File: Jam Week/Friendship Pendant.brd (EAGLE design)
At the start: 66 x 66 mm, 40 parts, among them IC1 LM556D, IC2 LM556D, IC3 74AHC1G32DCK

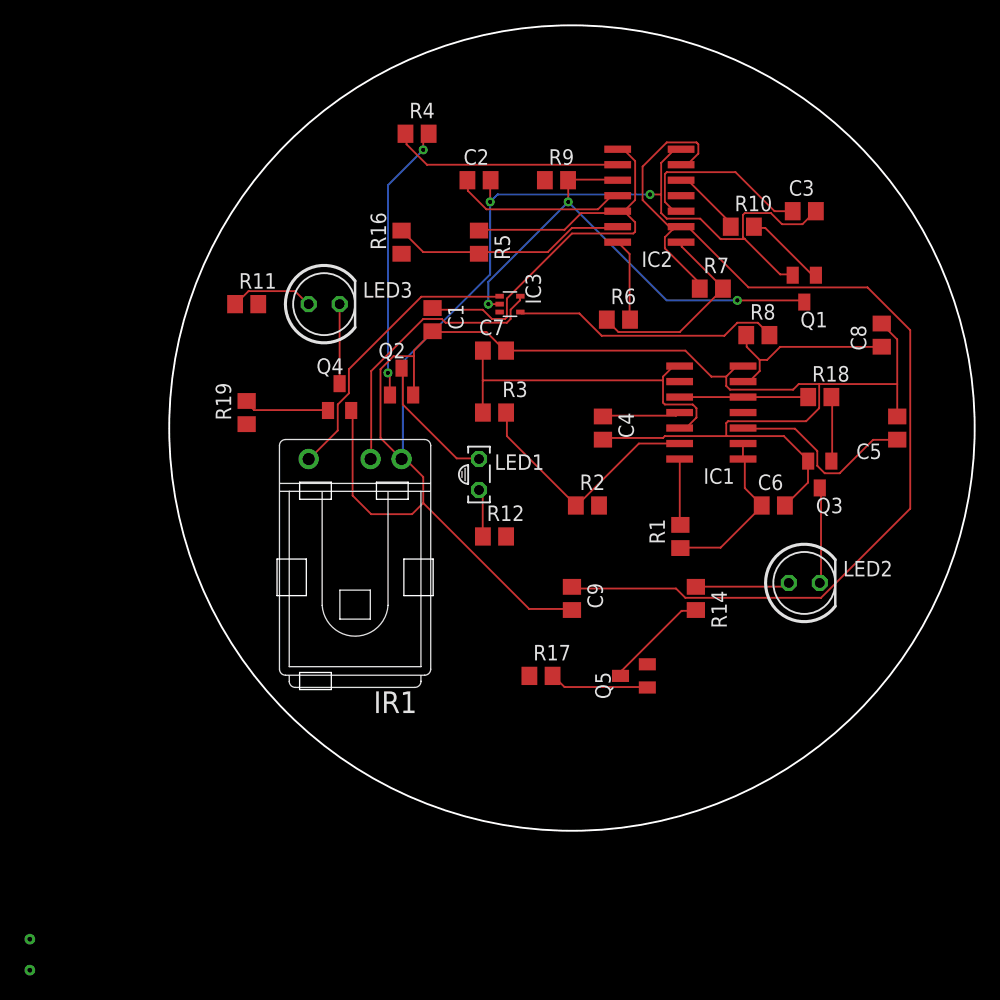
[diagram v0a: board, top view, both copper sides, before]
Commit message: Next class resolve air wire
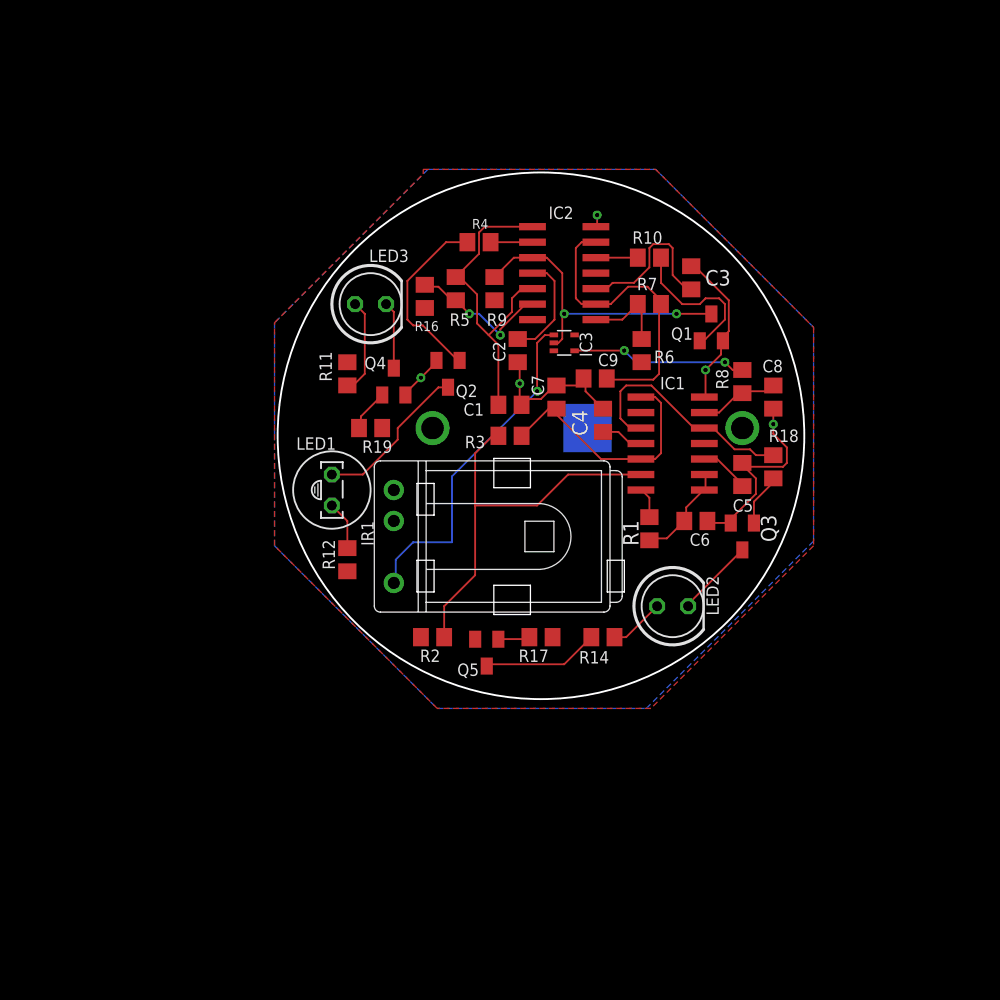
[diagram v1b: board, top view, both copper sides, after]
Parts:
- removed TP1, TP2: TEST-POINTTP_15TH_THRU, SparkFun-Connectors:TP_15TH
- added U1: 3039, 3039:3039
- moved C9 18.1 mm to (51.4, 51.1), turned to 180 degrees
- moved R2 16.7 mm to (38.1, 29.8), turned to 180 degrees
- moved C2 14.3 mm to (45.1, 53.3), turned to 270 degrees
- moved C5 13.3 mm to (63.5, 43.2)
- moved R12 12.2 mm to (31.1, 36.2), turned to 270 degrees
- moved Q5 12.2 mm to (42.5, 28.6), turned to 180 degrees
- moved LED1 12.1 mm to (29.8, 41.9)
- moved LED2 11.0 mm to (57.8, 32.4)
- moved C3 10.8 mm to (59.3, 59.3), turned to 90 degrees
- moved R4 10.2 mm to (41.9, 62.2), turned to 180 degrees
- moved R19 10.2 mm to (33.0, 47.0), turned to 180 degrees
- moved C8 10.2 mm to (66.0, 49.5), turned to 270 degrees
- moved R9 10.2 mm to (43.2, 58.4), turned to 90 degrees
- moved R11 10.0 mm to (31.1, 51.4), turned to 90 degrees
- moved IC2 9.44 mm to (48.9, 59.7)
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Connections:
- removed net N$15: IC2.14, R6.2
- removed net N$20: R12.2
- removed net N$22: IC1.4
- removed net N$25: R2.2
- removed net N$33: Q5.2
- removed net N$37: R16.1
- removed net N$38: R11.2
- removed net N$39: TP1.P$1
- net 0: now also U1.3; no longer TP2.P$1
- net VCC: now also IC1.4, IC2.14, Q5.2, R11.2, R12.2, R16.1, R2.2, R6.2, R9.1, U1.1, U1.2
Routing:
- net 0: track 203.6 -> 49.7 mm, vias 2 -> 5
- net N$16: track 90.2 -> 24.9 mm
- net VCC: track 22.9 -> 0.00 mm
- net N$4: track 40.8 -> 25.2 mm, vias 3 -> 2
- net SIGNAL: track 18.9 -> 3.44 mm
- net N$35: track 41.9 -> 27.0 mm
- net N$1: track 20.6 -> 33.3 mm
- net N$18: track 16.0 -> 4.13 mm
- net N$2: track 16.7 -> 7.04 mm
- net ENABLE: track 10.5 -> 19.3 mm
- net N$17: track 15.6 -> 6.76 mm
- net N$24: track 29.2 -> 21.2 mm
- net N$10: track 22.9 -> 15.1 mm, vias 2 -> 0
- net N$3: track 22.1 -> 14.4 mm, vias 0 -> 2
- net N$36: track 19.4 -> 12.1 mm, vias 0 -> 2
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- added copper zone on layer 16, net 0
- added copper zone on layer 1, net VCC
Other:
- board size 66 x 66 mm -> 43.2 x 43.2 mm

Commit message: Almost done,
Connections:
- removed net N$26: R19.1
- removed net N$32: R17.1
- net BLINK: now also R17.1, R19.1
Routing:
- net BLINK: track 0.00 -> 42.8 mm, vias 0 -> 3
- net ENABLE: track 19.3 -> 15.2 mm, vias 0 -> 2
- net 0: track 49.7 -> 45.5 mm, vias 5 -> 6
- net N$16: track 24.9 -> 22.0 mm
- net N$24: track 21.2 -> 22.7 mm
- net N$11: track 28.1 -> 28.6 mm, vias 1 -> 0

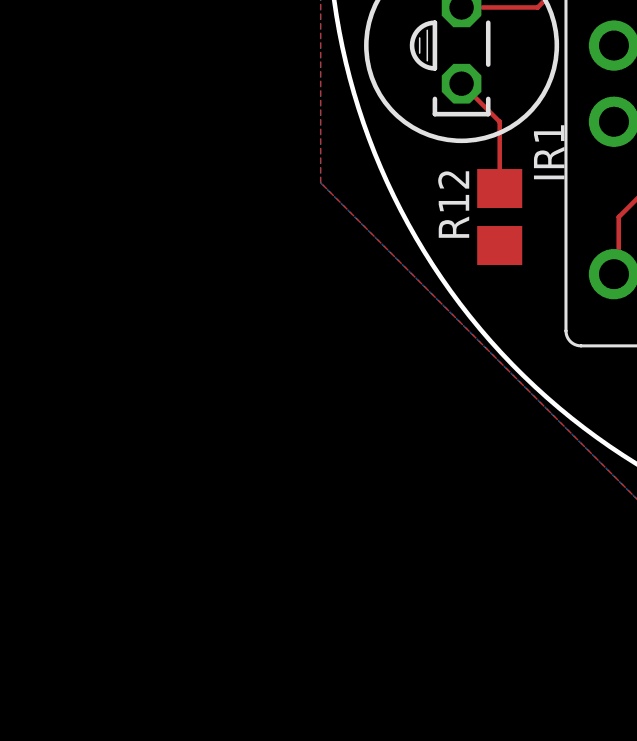
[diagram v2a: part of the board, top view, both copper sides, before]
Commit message: added switch and ordered without switch
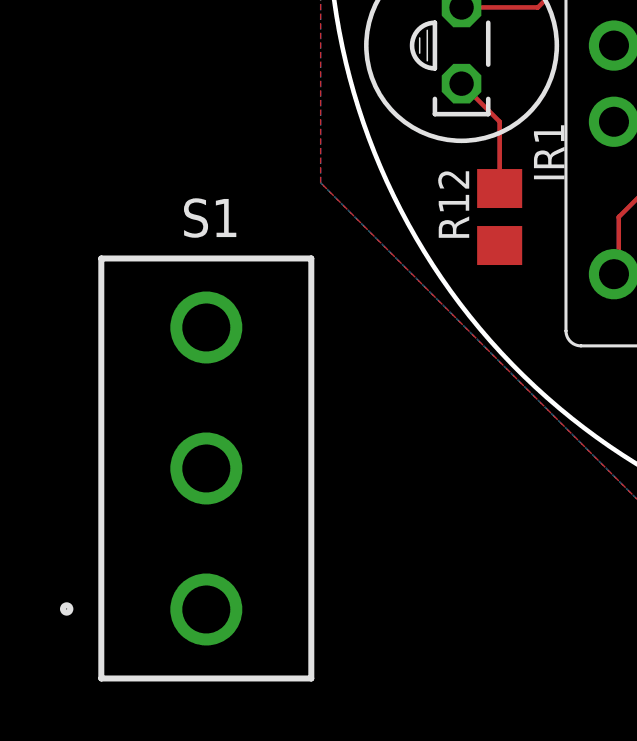
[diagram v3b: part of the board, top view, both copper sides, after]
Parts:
- added S1: CS12ANW03, CS12ANW03:CS12ANW03
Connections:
- new net N$15: S1.2, U1.1, U1.2
- net VCC: now also S1.3; no longer U1.1, U1.2
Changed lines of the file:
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@@
 <attribute name="VALUE" x="51.251" y="48.316" size="1.27" layer="28" rot="MR0" align="center"/>
+</element>
+<element name="S1" library="CS12ANW03" package="CS12ANW03" value="CS12ANW03" x="21.336" y="27.813" smashed="yes">
+<attribute name="ALLIED_NUMBER" value="70228233" x="21.336" y="27.813" size="1.778" layer="27" display="off"/>
+<attribute name="ALLIED_PRICE-STOCK" value="https://www.alliedelec.com/nkk-switches-cs12anw03/70228233/" x="21.336" y="27.813" size="1.778" layer="27" display="off"/>
+<attribute name="DESCRIPTION" value="NKK SWITCHES - CS12ANW03 - SWITCH, SLIDE, SPDT, 3A, 250V, TH" x="21.336" y="27.813" size="1.778" layer="27" display="off"/>
+<attribute name="HEIGHT" value="mm" x="21.336" y="27.813" size="1.778" layer="27" display="off"/>
+<attribute name="MANUFACTURER_NAME" value="NKK Switches" x="21.336" y="27.813" size="1.778" layer="27" display="off"/>
+<attribute name="MANUFACTURER_PART_NUMBER" value="CS12ANW03" x="21.336" y="27.813" size="1.778" layer="27" display="off"/>
+<attribute name="MOUSER_PART_NUMBER" value="633-CS12ANW03" x="21.336" y="27.813" size="1.778" layer="27" display="off"/>
+<attribute name="MOUSER_PRICE-STOCK" value="https://www.mouser.com/Search/Refine.aspx?Keyword=633-CS12ANW03" x="21.336" y="27.813" size="1.778" layer="27" display="off"/>
+<attribute name="NAME" x="21.484" y="36.162" size="1.27" layer="25" align="center"/>
+<attribute name="RS_PART_NUMBER" value="1251847" x="21.336" y="27.813" size="1.778" layer="27" display="off"/>
+<attribute name="RS_PRICE-STOCK" value="http://uk.rs-online.com/web/p/products/1251847" x="21.336" y="27.813" size="1.778" layer="27" display="off"/>
+<attribute name="VALUE" x="20.722" y="35.781" size="1.27" layer="27" align="center"/>
 </element>
 </elements>
@@
 <contactref element="IC3" pad="5"/>
 <contactref element="IR1" pad="VS"/>
-<contactref element="U1" pad="1"/>
-<contactref element="U1" pad="2"/>
 <contactref element="R9" pad="1"/>
 <contactref element="R12" pad="2"/>
@@
 <contactref element="IC2" pad="14"/>
 <contactref element="R6" pad="2"/>
+<contactref element="S1" pad="3"/>
+<wire x1="55.245" y1="52.39" x2="60.385" y2="45.72" width="0" layer="19" extent="1-1"/>
+<wire x1="49.745" y1="54.625" x2="55.245" y2="52.39" width="0" layer="19" extent="1-1"/>
+<wire x1="46.295" y1="55.88" x2="49.745" y2="54.625" width="0" layer="19" extent="1-1"/>
+<wire x1="43.18" y1="57.47" x2="46.295" y2="55.88" width="0" layer="19" extent="1-1"/>
+<wire x1="37.465" y1="56.835" x2="43.18" y2="57.47" width="0" layer="19" extent="1-1"/>
+<wire x1="31.115" y1="52.385" x2="37.465" y2="56.835" width="0" layer="19" extent="1-1"/>
+<wire x1="34.925" y1="39.37" x2="31.115" y2="52.385" width="0" layer="19" extent="1-1"/>
+<wire x1="31.115" y1="35.245" x2="34.925" y2="39.37" width="0" layer="19" extent="1-1"/>
+<wire x1="37.15" y1="29.845" x2="31.115" y2="35.245" width="0" layer="19" extent="1-1"/>
+<wire x1="41.595" y1="29.675" x2="37.15" y2="29.845" width="0" layer="19" extent="1-1"/>
+<wire x1="21.336" y1="32.513" x2="31.115" y2="35.245" width="0" layer="19" extent="1-1"/>
 </signal>
 <signal name="N$1">
@@
 <wire x1="46.295" y1="62.23" x2="42.86" y2="62.23" width="0.1524" layer="1"/>
 </signal>
+<signal name="N$15">
+<contactref element="U1" pad="1"/>
+<contactref element="U1" pad="2"/>
+<contactref element="S1" pad="2"/>
+<wire x1="38.1" y1="46.99" x2="63.5" y2="46.99" width="0" layer="19" extent="1-1"/>
+<wire x1="21.336" y1="27.813" x2="38.1" y2="46.99" width="0" layer="19" extent="1-1"/>
+</signal>
 </signals>

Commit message: final day
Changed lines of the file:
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@@
 <attribute name="MOUSER#" value="595-SN74AUP1G32DCKR" x="18.415" y="28.575" size="1.778" layer="27" rot="R270" display="off"/>
 <attribute name="MPN" value="SN74AUP1G32DCKR" x="18.415" y="28.575" size="1.778" layer="27" rot="R270" display="off"/>
-<attribute name="NAME" x="50.165" y="54.864" size="1.016" layer="25" rot="R270"/>
+<attribute name="NAME" x="50.165" y="56.515" size="1.27" layer="25" rot="R270"/>
 <attribute name="VALUE" x="46.355" y="56.515" size="1.27" layer="27" rot="R270"/>
 </element>
@@
 <contactref element="R6" pad="2"/>
 <contactref element="S1" pad="3"/>
-<wire x1="55.245" y1="52.39" x2="60.385" y2="45.72" width="0" layer="19" extent="1-1"/>
-<wire x1="49.745" y1="54.625" x2="55.245" y2="52.39" width="0" layer="19" extent="1-1"/>
-<wire x1="46.295" y1="55.88" x2="49.745" y2="54.625" width="0" layer="19" extent="1-1"/>
-<wire x1="43.18" y1="57.47" x2="46.295" y2="55.88" width="0" layer="19" extent="1-1"/>
-<wire x1="37.465" y1="56.835" x2="43.18" y2="57.47" width="0" layer="19" extent="1-1"/>
-<wire x1="31.115" y1="52.385" x2="37.465" y2="56.835" width="0" layer="19" extent="1-1"/>
-<wire x1="34.925" y1="39.37" x2="31.115" y2="52.385" width="0" layer="19" extent="1-1"/>
-<wire x1="31.115" y1="35.245" x2="34.925" y2="39.37" width="0" layer="19" extent="1-1"/>
-<wire x1="37.15" y1="29.845" x2="31.115" y2="35.245" width="0" layer="19" extent="1-1"/>
-<wire x1="41.595" y1="29.675" x2="37.15" y2="29.845" width="0" layer="19" extent="1-1"/>
-<wire x1="21.336" y1="32.513" x2="31.115" y2="35.245" width="0" layer="19" extent="1-1"/>
+<wire x1="31.115" y1="35.245" x2="21.336" y2="32.513" width="0" layer="19" extent="1-1"/>
 </signal>
 <signal name="N$1">
